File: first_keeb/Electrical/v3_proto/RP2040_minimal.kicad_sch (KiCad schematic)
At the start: 61 parts, among them J1 Conn_01x05_Socket, J2 Conn_01x01_Socket, P1 USB4105-GF-A, Q1 BSS138, SW1 SW_Push, SW2 SW_Push, U1 NCP1117-3.3_SOT223, U2 LM4040DBZ-3, U3 PRTR5V0U2X, U4 W25Q32JVSS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

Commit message: finishes circular pcb
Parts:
- removed D1, D2, D3, D4: WS2812B, LED_SMD:LED_WS2812B_PLCC4_5.0x5.0mm_P3.2mm, symbol LED:WS2812B
- removed D5, D6, D7: SK6812MINI, LED_SMD:LED_SK6812MINI_PLCC4_3.5x3.5mm_P1.75mm, symbol LED:SK6812MINI
- removed J1: Conn_01x05_Socket, Connector_PinSocket_2.54mm:PinSocket_1x05_P2.54mm_Vertical, symbol Connector:Conn_01x05_Socket
- removed J2: Conn_01x01_Socket, Connector_PinSocket_2.54mm:PinSocket_1x01_P2.54mm_Vertical, symbol Connector:Conn_01x01_Socket
- added C29: 100n, Capacitor_SMD:C_0402_1005Metric, symbol Device:C
- added D1, D2, D3, D4, D5, D6, D7, D8: WS2812B-2020, LED_SMD:LED_WS2812B-2020_PLCC4_2.0x2.0mm, symbol LED:WS2812B-2020
- C22, C23, C24, C25, C26, C27, C28: value 1u -> 100n
- SW1, SW2: now fitted
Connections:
- net +5V: now also C29.1, D1.4 (VDD), D2.4 (VDD), D3.4 (VDD), D4.4 (VDD), D5.4 (VDD), D6.4 (VDD), D7.4 (VDD), D8.4 (VDD)
- net BUTT0: no longer U5.13 (GPIO10)
- net BUTT1: no longer U5.14 (GPIO11)
- net GND: now also C29.2, D1.2 (GND), D2.2 (GND), D3.2 (GND), D4.2 (GND), D5.2 (GND), D6.2 (GND), D7.2 (GND), D8.2 (GND)
- net LED_D_5V: now also D1.3 (DIN)
- net USB_D+: now also U3.3 (I/O2); no longer U3.2 (I/O1)
- net USB_D-: now also U3.2 (I/O1); no longer U3.3 (I/O2)
- net UART0 renamed GPIO16
- net UART1 renamed GPIO17
- new net: D1.1 (DOUT), D2.3 (DIN)
- new net: D7.1 (DOUT), D8.3 (DIN)
- new net: D5.1 (DOUT), D6.3 (DIN)
- new net: D4.1 (DOUT), D5.3 (DIN)
- new net: D3.1 (DOUT), D4.3 (DIN)
- new net: D2.1 (DOUT), D3.3 (DIN)
- new net: D6.1 (DOUT), D7.3 (DIN)
- new net GPIO10: U5.13 (GPIO10)
- new net GPIO11: U5.14 (GPIO11)
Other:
- moved on the sheet: U3

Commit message: finishes pcb even more
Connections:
- net BUTT0 is gone; now on net GPIO18: SW1.1
- net BUTT1 is gone; now on net GPIO19: SW2.1
- net GPIO12: no longer Q1.2 (S), R9.2
- net GPIO17: now also Q1.2 (S), R9.2
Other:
- note added: "Underglow"
- note removed: "Backlight/Underglow LED"
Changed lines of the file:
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@@
     (effects (font (size 2 2)) (justify left bottom))
   )
-  (text "Backlight/Underglow LED" (at 176.53 198.755 0)
+  (text "Underglow" (at 176.53 198.755 0)
     (effects (font (size 2 2)) (justify left bottom))
   )
@@
     )
   )
-  (global_label "GPIO12" (shape input) (at 153.035 226.06 180) (fields_autoplaced)
+  (global_label "GPIO17" (shape input) (at 153.035 226.06 180) (fields_autoplaced)
     (effects (font (size 1.27 1.27)) (justify right))
     (property "Intersheetrefs" "${INTERSHEET_REFS}" (at 143.8891 226.06 0)
@@
     )
   )
-  (global_label "BUTT1" (shape input) (at 67.31 271.78 180) (fields_autoplaced)
-    (effects (font (size 1.27 1.27)) (justify right))
-    (property "Intersheetrefs" "${INTERSHEET_REFS}" (at 59.3132 271.78 0)
+  (global_label "GPIO19" (shape input) (at 67.31 271.78 180) (fields_autoplaced)
+    (effects (font (size 1.27 1.27)) (justify right))
+    (property "Intersheetrefs" "${INTERSHEET_REFS}" (at 58.1641 271.78 0)
       (effects (font (size 1.27 1.27)) (justify right) hide)
     )
@@
     )
   )
-  (global_label "BUTT0" (shape input) (at 67.31 257.175 180) (fields_autoplaced)
-    (effects (font (size 1.27 1.27)) (justify right))
-    (property "Intersheetrefs" "${INTERSHEET_REFS}" (at 59.3132 257.175 0)
-      (effects (font (size 1.27 1.27)) (justify right) hide)
-    )
+  (global_label "GPIO18" (shape input) (at 67.31 257.175 180) (fields_autoplaced)
+    (effects (font (size 1.27 1.27)) (justify right))
+    (property "Intersheetrefs" "${INTERSHEET_REFS}" (at 58.1641 257.175 0)
+      (effects (font (size 1.27 1.27)) (justify right) hide)
+    )

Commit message: ads bootsel button and changes pcb to 80mm diameter
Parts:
- removed Q1: BSS138, Package_TO_SOT_SMD:SOT-23, symbol Transistor_FET:BSS138
- removed R10, R9: 10k, Capacitor_SMD:C_0402_1005Metric, symbol Device:R
- added Q1: SN74LV1T34DBV, Package_TO_SOT_SMD:SOT-23-5, symbol Logic_LevelTranslator:SN74LV1T34DBV
- added SW3: SKRKAGE020, Button_Switch_SMD:SW_Push_SPST_NO_Alps_SKRK, symbol Switch:SW_Push
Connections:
- net +5V: now also Q1.5 (VCC)
- net GND: now also Q1.3 (GND), SW3.1
- net GPIO17: now also Q1.2 (A)
- net LED_D_5V: now also Q1.4 (Y)
- net QSPI_SS: now also SW3.2
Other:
- note added: "BOOTSEL"

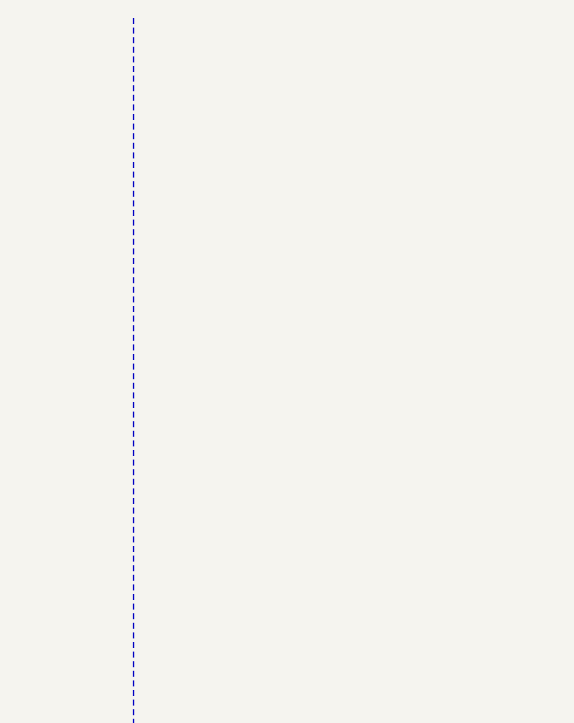
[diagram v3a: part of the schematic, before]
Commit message: ads threaded mounting hole
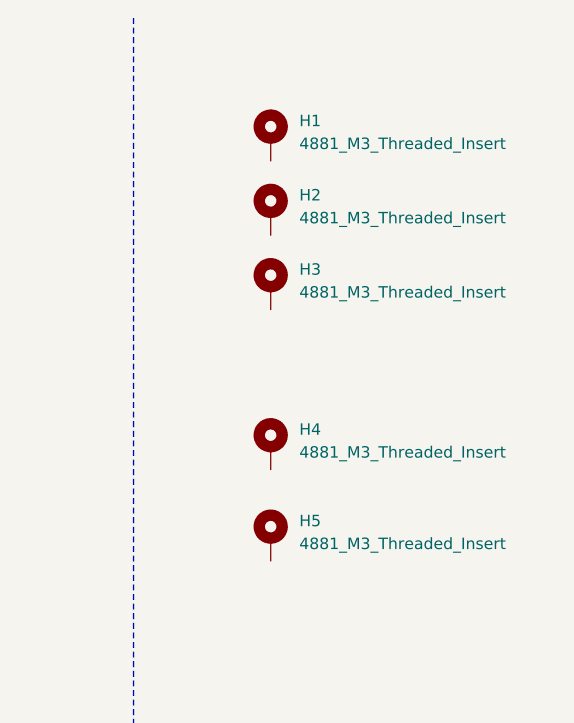
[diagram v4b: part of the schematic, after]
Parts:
- added H1, H2, H3, H4, H5: 4881_M3_Threaded_Insert, MountingHole:4881_M3_Threaded_Insert, symbol Mechanical:4881
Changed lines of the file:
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@@
+    )
+  )
+  (symbol (lib_id "Mechanical:4881") (at 351.155 33.655 0) (unit 1)
+    (in_bom yes) (on_board yes) (dnp no) (fields_autoplaced)
+    (property "Reference" "H2" (at 354.33 31.75 0)
+      (effects (font (size 1.27 1.27)) (justify left))
+    )
+    (property "Value" "4881_M3_Threaded_Insert" (at 354.33 34.29 0)
+      (effects (font (size 1.27 1.27)) (justify left))
+    )
+    (property "Footprint" "MountingHole:4881_M3_Threaded_Insert" (at 351.155 33.655 0)
+      (effects (font (size 1.27 1.27)) hide)
+    )
+    (property "Datasheet" "~" (at 351.155 33.655 0)
+      (effects (font (size 1.27 1.27)) hide)
+    )
+    (pin "1")
+    (instances
+      (project "RP2040_minimal"
+        (path "/26e500cb-9f3f-4e62-bb26-21a6be4a5bcc"
+          (reference "H2") (unit 1)
+        )
+      )
     )
   )
@@
         (path "/26e500cb-9f3f-4e62-bb26-21a6be4a5bcc"
           (reference "#PWR028") (unit 1)
+        )
+      )
+    )
+  )
+  (symbol (lib_id "Mechanical:4881") (at 351.155 41.91 0) (unit 1)
+    (in_bom yes) (on_board yes) (dnp no) (fields_autoplaced)
+    (property "Reference" "H3" (at 354.33 40.005 0)
+      (effects (font (size 1.27 1.27)) (justify left))
+    )
+    (property "Value" "4881_M3_Threaded_Insert" (at 354.33 42.545 0)
+      (effects (font (size 1.27 1.27)) (justify left))
+    )
+    (property "Footprint" "MountingHole:4881_M3_Threaded_Insert" (at 351.155 41.91 0)
+      (effects (font (size 1.27 1.27)) hide)
+    )
+    (property "Datasheet" "~" (at 351.155 41.91 0)
+      (effects (font (size 1.27 1.27)) hide)
+    )
+    (pin "1")
+    (instances
+      (project "RP2040_minimal"
+        (path "/26e500cb-9f3f-4e62-bb26-21a6be4a5bcc"
+          (reference "H3") (unit 1)
         )
       )
@@
     )
   )
+  (symbol (lib_id "Mechanical:4881") (at 351.155 69.85 0) (unit 1)
+    (in_bom yes) (on_board yes) (dnp no) (fields_autoplaced)
+    (property "Reference" "H5" (at 354.33 67.945 0)
+      (effects (font (size 1.27 1.27)) (justify left))
+    )
+    (property "Value" "4881_M3_Threaded_Insert" (at 354.33 70.485 0)
+      (effects (font (size 1.27 1.27)) (justify left))
+    )
+    (property "Footprint" "MountingHole:4881_M3_Threaded_Insert" (at 351.155 69.85 0)
+      (effects (font (size 1.27 1.27)) hide)
+    )
+    (property "Datasheet" "~" (at 351.155 69.85 0)
+      (effects (font (size 1.27 1.27)) hide)
+    )
+    (pin "1")
+    (instances
+      (project "RP2040_minimal"
+        (path "/26e500cb-9f3f-4e62-bb26-21a6be4a5bcc"
+          (reference "H5") (unit 1)
+        )
+      )
+    )
+  )
   (symbol (lib_id "power:VBUS") (at 248.92 30.48 0) (unit 1)
     (in_bom yes) (on_board yes) (dnp no)
@@
         (path "/26e500cb-9f3f-4e62-bb26-21a6be4a5bcc"
           (reference "C23") (unit 1)
+        )
+      )
+    )
+  )
+  (symbol (lib_id "Mechanical:4881") (at 351.155 59.69 0) (unit 1)
+    (in_bom yes) (on_board yes) (dnp no) (fields_autoplaced)
+    (property "Reference" "H4" (at 354.33 57.785 0)
+      (effects (font (size 1.27 1.27)) (justify left))
+    )
+    (property "Value" "4881_M3_Threaded_Insert" (at 354.33 60.325 0)
+      (effects (font (size 1.27 1.27)) (justify left))
+    )
+    (property "Footprint" "MountingHole:4881_M3_Threaded_Insert" (at 351.155 59.69 0)
+      (effects (font (size 1.27 1.27)) hide)
+    )
+    (property "Datasheet" "~" (at 351.155 59.69 0)
+      (effects (font (size 1.27 1.27)) hide)
+    )
+    (pin "1")
+    (instances
+      (project "RP2040_minimal"
+        (path "/26e500cb-9f3f-4e62-bb26-21a6be4a5bcc"
+          (reference "H4") (unit 1)
         )
       )
@@
         )
       )
+    )
+  )
+  (symbol (lib_id "Mechanical:4881") (at 351.155 25.4 0) (unit 1)
+    (in_bom yes) (on_board yes) (dnp no) (fields_autoplaced)
+    (property "Reference" "H1" (at 354.33 23.495 0)
+      (effects (font (size 1.27 1.27)) (justify left))
+    )
+    (property "Value" "4881_M3_Threaded_Insert" (at 354.33 26.035 0)
+      (effects (font (size 1.27 1.27)) (justify left))
+    )
+    (property "Footprint" "MountingHole:4881_M3_Threaded_Insert" (at 351.155 25.4 0)
+      (effects (font (size 1.27 1.27)) hide)
+    )
+    (property "Datasheet" "~" (at 351.155 25.4 0)
+      (effects (font (size 1.27 1.27)) hide)
+    )
+    (pin "1")
+    (instances
+      (project "RP2040_minimal"
+        (path "/26e500cb-9f3f-4e62-bb26-21a6be4a5bcc"
+          (reference "H1") (unit 1)
+        )
+      )
